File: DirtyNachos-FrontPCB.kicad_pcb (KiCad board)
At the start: 2 copper layers, 18.5 x 107.5 mm, 19 parts, among them J1 OUTPUT, J2 INPUT, J3 CV IN, P10F1 Conn_01x01_Socket, P1F1 Conn_01x01_Socket, P2F1 Conn_01x01_Socket, P3F1 Conn_01x01_Socket, P4F1 Conn_01x01_Socket, P5F1 Conn_01x01_Socket, P7F1 Conn_01x01_Socket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

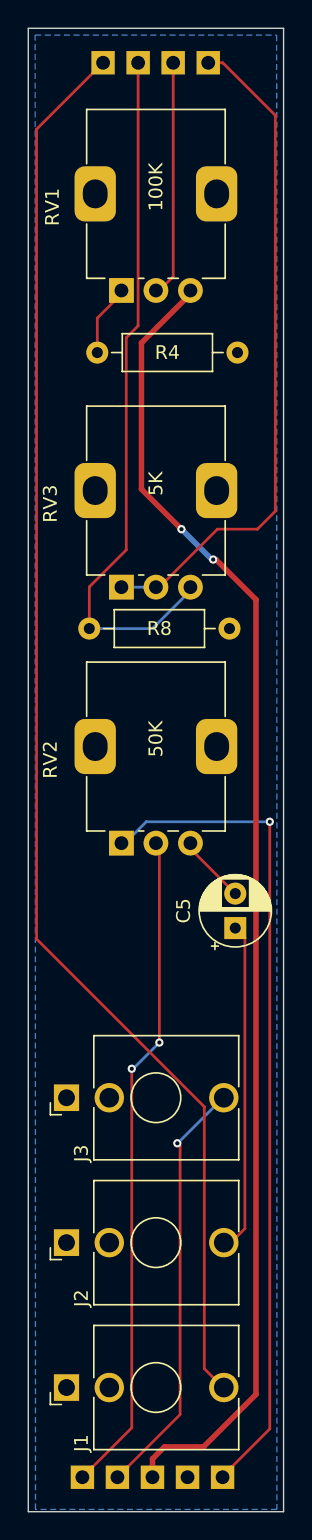
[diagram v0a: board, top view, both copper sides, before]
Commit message: V0.2
Fixed Tracks. Now they are wider. And optimized routes.
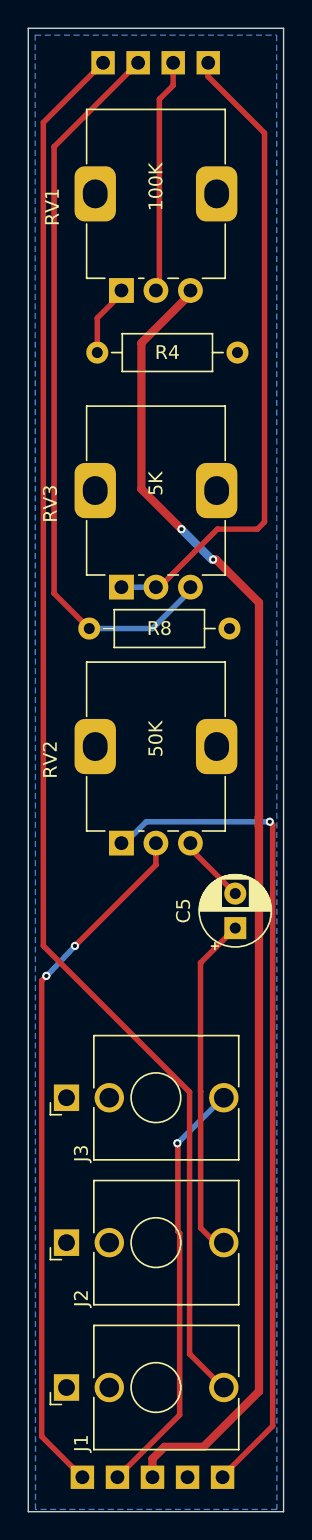
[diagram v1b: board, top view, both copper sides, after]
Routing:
- net Net-(P3F1-Pin_1): track 51.6 -> 53.4 mm
- net Net-(P1F1-Pin_1): track 48.3 -> 47.0 mm
- net Net-(C5-Pad1): track 24.3 -> 25.1 mm
- net Net-(P5F1-Pin_1): track 48.3 -> 47.6 mm
